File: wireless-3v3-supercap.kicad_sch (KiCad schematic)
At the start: 5 parts

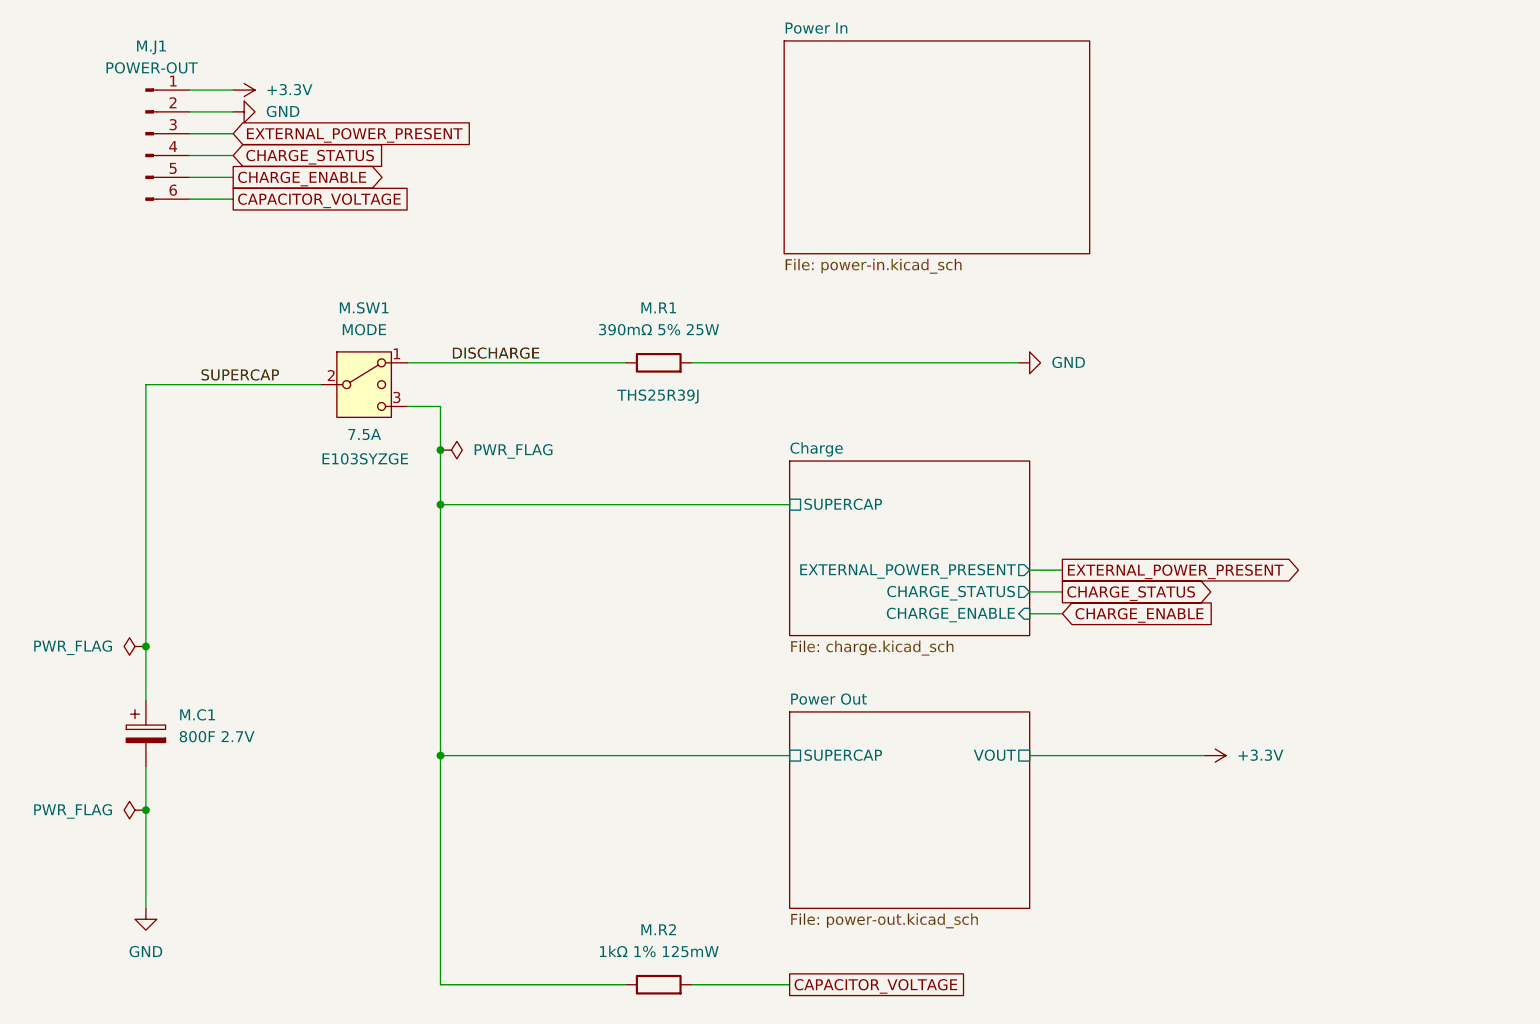
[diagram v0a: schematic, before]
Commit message: Remove charge enable pin
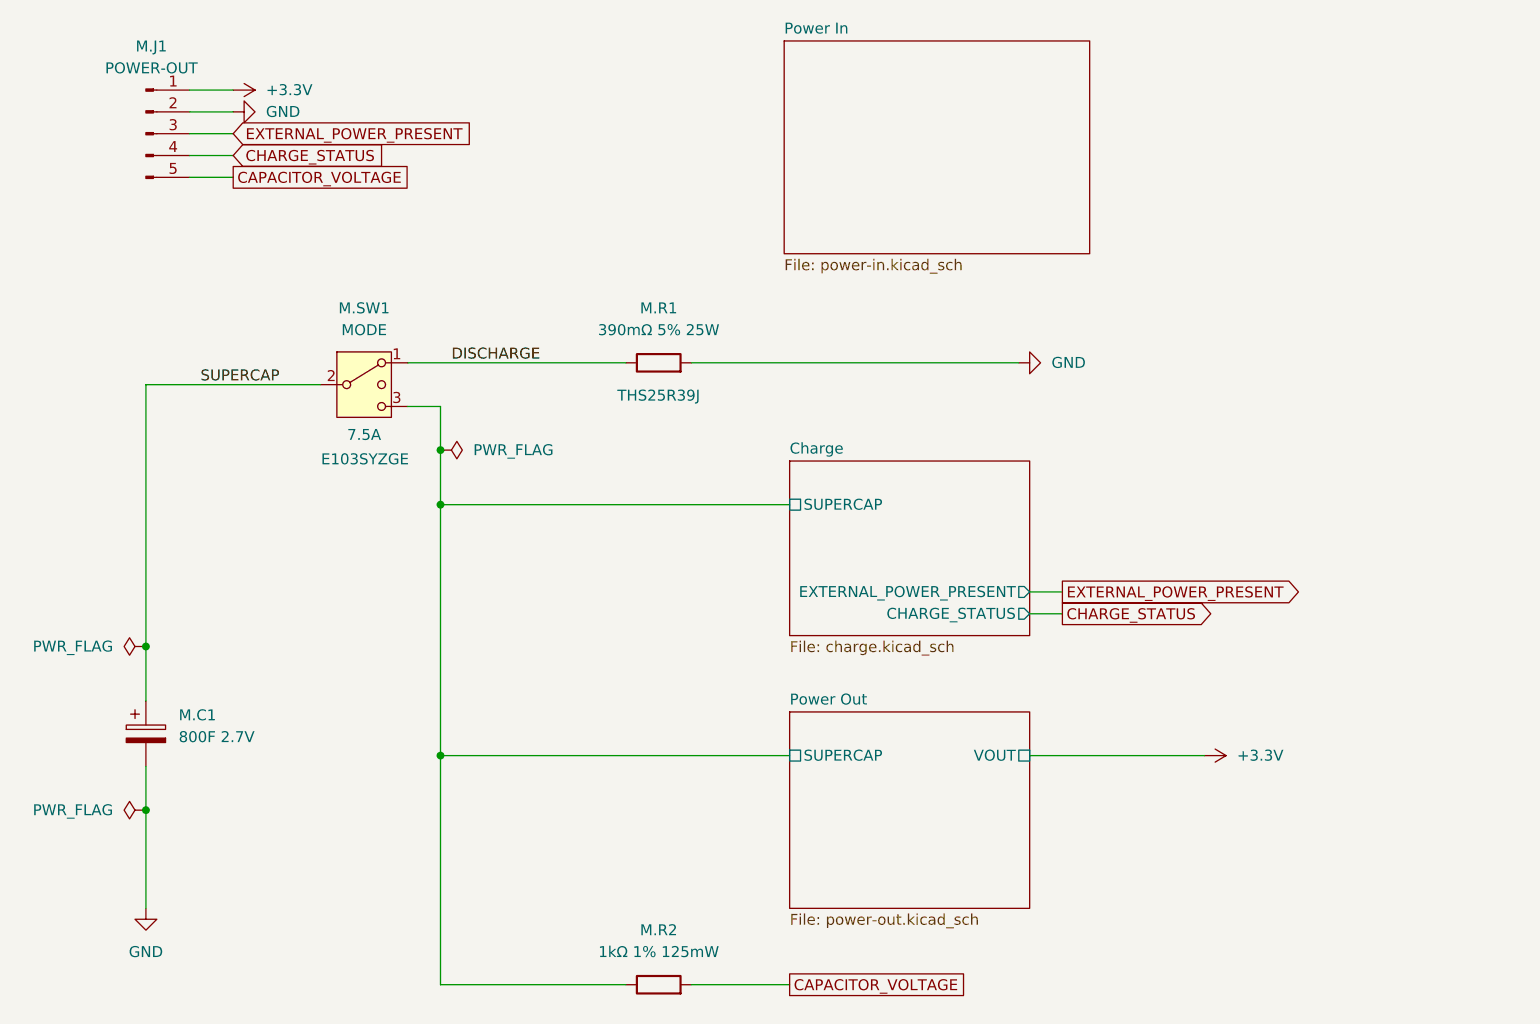
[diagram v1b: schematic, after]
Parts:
- M.J1: footprint Connector_PinHeader_2.54mm:PinHeader_1x06_P2.54mm_Vertical -> Connector_PinHeader_2.54mm:PinHeader_1x05_P2.54mm_Vertical; symbol Connector:Conn_01x06_Pin -> Connector:Conn_01x05_Pin
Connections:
- net CHARGE_ENABLE is gone; now on net CAPACITOR_VOLTAGE: M.J1.5 (Pin_5)
- net CAPACITOR_VOLTAGE: no longer M.J1.6 (Pin_6)
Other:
- sheet Charge ports: added none; removed CHARGE_ENABLE
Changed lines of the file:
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@@
-	(wire
-		(pts
-			(xy 30.48 27.94) (xy 35.56 27.94)
-		)
-		(stroke
-			(width 0)
-			(type default)
-		)
-	)
 	(wire
 		(pts
@@
 	(wire
 		(pts
+			(xy 59.69 63.5) (xy 100.33 63.5)
+		)
+		(stroke
+			(width 0)
+			(type default)
+		)
+	)
+	(wire
+		(pts
+			(xy 30.48 25.4) (xy 35.56 25.4)
+		)
+		(stroke
+			(width 0)
+			(type default)
+		)
+	)
+	(wire
+		(pts
+			(xy 25.4 80.01) (xy 25.4 86.36)
+		)
+		(stroke
+			(width 0)
+			(type default)
+		)
+	)
+	(wire
+		(pts
+			(xy 128.27 73.66) (xy 132.08 73.66)
+		)
+		(stroke
+			(width 0)
+			(type default)
+		)
+	)
+	(wire
+		(pts
+			(xy 30.48 15.24) (xy 35.56 15.24)
+		)
+		(stroke
+			(width 0)
+			(type default)
+		)
+	)
+	(wire
+		(pts
+			(xy 128.27 92.71) (xy 148.59 92.71)
+		)
+		(stroke
+			(width 0)
+			(type default)
+		)
+	)
+	(wire
+		(pts
 			(xy 128.27 76.2) (xy 132.08 76.2)
-		)
-		(stroke
-			(width 0)
-			(type default)
-		)
-	)
-	(wire
-		(pts
-			(xy 59.69 63.5) (xy 100.33 63.5)
-		)
-		(stroke
-			(width 0)
-			(type default)
-		)
-	)
-	(wire
-		(pts
-			(xy 30.48 25.4) (xy 35.56 25.4)
-		)
-		(stroke
-			(width 0)
-			(type default)
-		)
-	)
-	(wire
-		(pts
-			(xy 25.4 80.01) (xy 25.4 86.36)
-		)
-		(stroke
-			(width 0)
-			(type default)
-		)
-	)
-	(wire
-		(pts
-			(xy 128.27 71.12) (xy 132.08 71.12)
-		)
-		(stroke
-			(width 0)
-			(type default)
-		)
-	)
-	(wire
-		(pts
-			(xy 30.48 15.24) (xy 35.56 15.24)
-		)
-		(stroke
-			(width 0)
-			(type default)
-		)
-	)
-	(wire
-		(pts
-			(xy 128.27 92.71) (xy 148.59 92.71)
-		)
-		(stroke
-			(width 0)
-			(type default)
-		)
-	)
-	(wire
-		(pts
-			(xy 128.27 73.66) (xy 132.08 73.66)
 		)
 		(stroke
@@
 		)
 	)
-	(global_label "CHARGE_ENABLE"
-		(shape input)
-		(at 132.08 76.2 0)
+	(global_label "CAPACITOR_VOLTAGE"
+		(shape passive)
+		(at 100.33 119.38 0)
 		(fields_autoplaced yes)
 		(effects
@@
 		)
 		(property "Intersheetrefs" "${INTERSHEET_REFS}"
-			(at 150.4261 76.2 0)
-			(effects
-				(font
-					(size 1.27 1.27)
-				)
-				(justify left)
-				(hide yes)
-			)
-		)
-	)
-	(global_label "CAPACITOR_VOLTAGE"
-		(shape passive)
-		(at 100.33 119.38 0)
+			(at 121.254 119.38 0)
+			(effects
+				(font
+					(size 1.27 1.27)
+				)
+				(justify left)
+				(hide yes)
+			)
+		)
+	)
+	(global_label "EXTERNAL_POWER_PRESENT"
+		(shape output)
+		(at 132.08 73.66 0)
 		(fields_autoplaced yes)
 		(effects
@@
 		)
 		(property "Intersheetrefs" "${INTERSHEET_REFS}"
-			(at 121.254 119.38 0)
-			(effects
-				(font
-					(size 1.27 1.27)
-				)
-				(justify left)
-				(hide yes)
-			)
-		)
-	)
-	(global_label "EXTERNAL_POWER_PRESENT"
-		(shape output)
-		(at 132.08 71.12 0)
+			(at 161.0092 73.66 0)
+			(effects
+				(font
+					(size 1.27 1.27)
+				)
+				(justify left)
+				(hide yes)
+			)
+		)
+	)
+	(global_label "CHARGE_STATUS"
+		(shape input)
+		(at 35.56 22.86 0)
 		(fields_autoplaced yes)
 		(effects
@@
 		)
 		(property "Intersheetrefs" "${INTERSHEET_REFS}"
-			(at 161.0092 71.12 0)
+			(at 53.6642 22.86 0)
 			(effects
 				(font
@@
 	)
 	(global_label "CHARGE_STATUS"
-		(shape input)
-		(at 35.56 22.86 0)
+		(shape output)
+		(at 132.08 76.2 0)
 		(fields_autoplaced yes)
 		(effects
@@
 		)
 		(property "Intersheetrefs" "${INTERSHEET_REFS}"
-			(at 53.6642 22.86 0)
-			(effects
-				(font
-					(size 1.27 1.27)
-				)
-				(justify left)
-				(hide yes)
-			)
-		)
-	)
-	(global_label "CHARGE_STATUS"
-		(shape output)
-		(at 132.08 73.66 0)
+			(at 150.1842 76.2 0)
+			(effects
+				(font
+					(size 1.27 1.27)
+				)
+				(justify left)
+				(hide yes)
+			)
+		)
+	)
+	(global_label "CAPACITOR_VOLTAGE"
+		(shape passive)
+		(at 35.56 25.4 0)
 		(fields_autoplaced yes)
 		(effects
@@
 		)
 		(property "Intersheetrefs" "${INTERSHEET_REFS}"
-			(at 150.1842 73.66 0)
-			(effects
-				(font
-					(size 1.27 1.27)
-				)
-				(justify left)
-				(hide yes)
-			)
-		)
-	)
-	(global_label "CHARGE_ENABLE"
-		(shape output)
-		(at 35.56 25.4 0)
-		(fields_autoplaced yes)
-		(effects
-			(font
-				(size 1.27 1.27)
-			)
-			(justify left)
-		)
-		(property "Intersheetrefs" "${INTERSHEET_REFS}"
-			(at 53.9061 25.4 0)
-			(effects
-				(font
-					(size 1.27 1.27)
-				)
-				(justify left)
-				(hide yes)
-			)
-		)
-	)
-	(global_label "CAPACITOR_VOLTAGE"
-		(shape passive)
-		(at 35.56 27.94 0)
-		(fields_autoplaced yes)
-		(effects
-			(font
-				(size 1.27 1.27)
-			)
-			(justify left)
-		)
-		(property "Intersheetrefs" "${INTERSHEET_REFS}"
-			(at 56.484 27.94 0)
+			(at 56.484 25.4 0)
 			(effects
 				(font
@@
 	)
 	(symbol
-		(lib_id "Connector:Conn_01x06_Pin")
+		(lib_id "Connector:Conn_01x05_Pin")
 		(at 25.4 20.32 0)
 		(unit 1)
@@
 			)
 		)
-		(property "Footprint" "Connector_PinHeader_2.54mm:PinHeader_1x06_P2.54mm_Vertical"
+		(property "Footprint" "Connector_PinHeader_2.54mm:PinHeader_1x05_P2.54mm_Vertical"
 			(at 25.4 20.32 0)
 			(effects
@@
 			)
 		)
-		(property "Description" "Generic connector, single row, 01x06, script generated"
+		(property "Description" "Generic connector, single row, 01x05, script generated"
 			(at 25.4 20.32 0)
 			(effects
@@
 		)
 		(pin "5"
-		)
-		(pin "6"
 		)
 		(instances
@@
 			)
 		)
-		(pin "CHARGE_ENABLE" input
+		(pin "CHARGE_STATUS" output
 			(at 128.27 76.2 0)
 			(effects
@@
 			)
 		)
-		(pin "CHARGE_STATUS" output
+		(pin "EXTERNAL_POWER_PRESENT" output
 			(at 128.27 73.66 0)
 			(effects
 				(font
-					(size 1.27 1.27)
-				)
-				(justify right)
-			)
-		)
-		(pin "EXTERNAL_POWER_PRESENT" output
-			(at 128.27 71.12 0)
-			(effects
-				(font

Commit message: Add voltage divider circuit for ADC
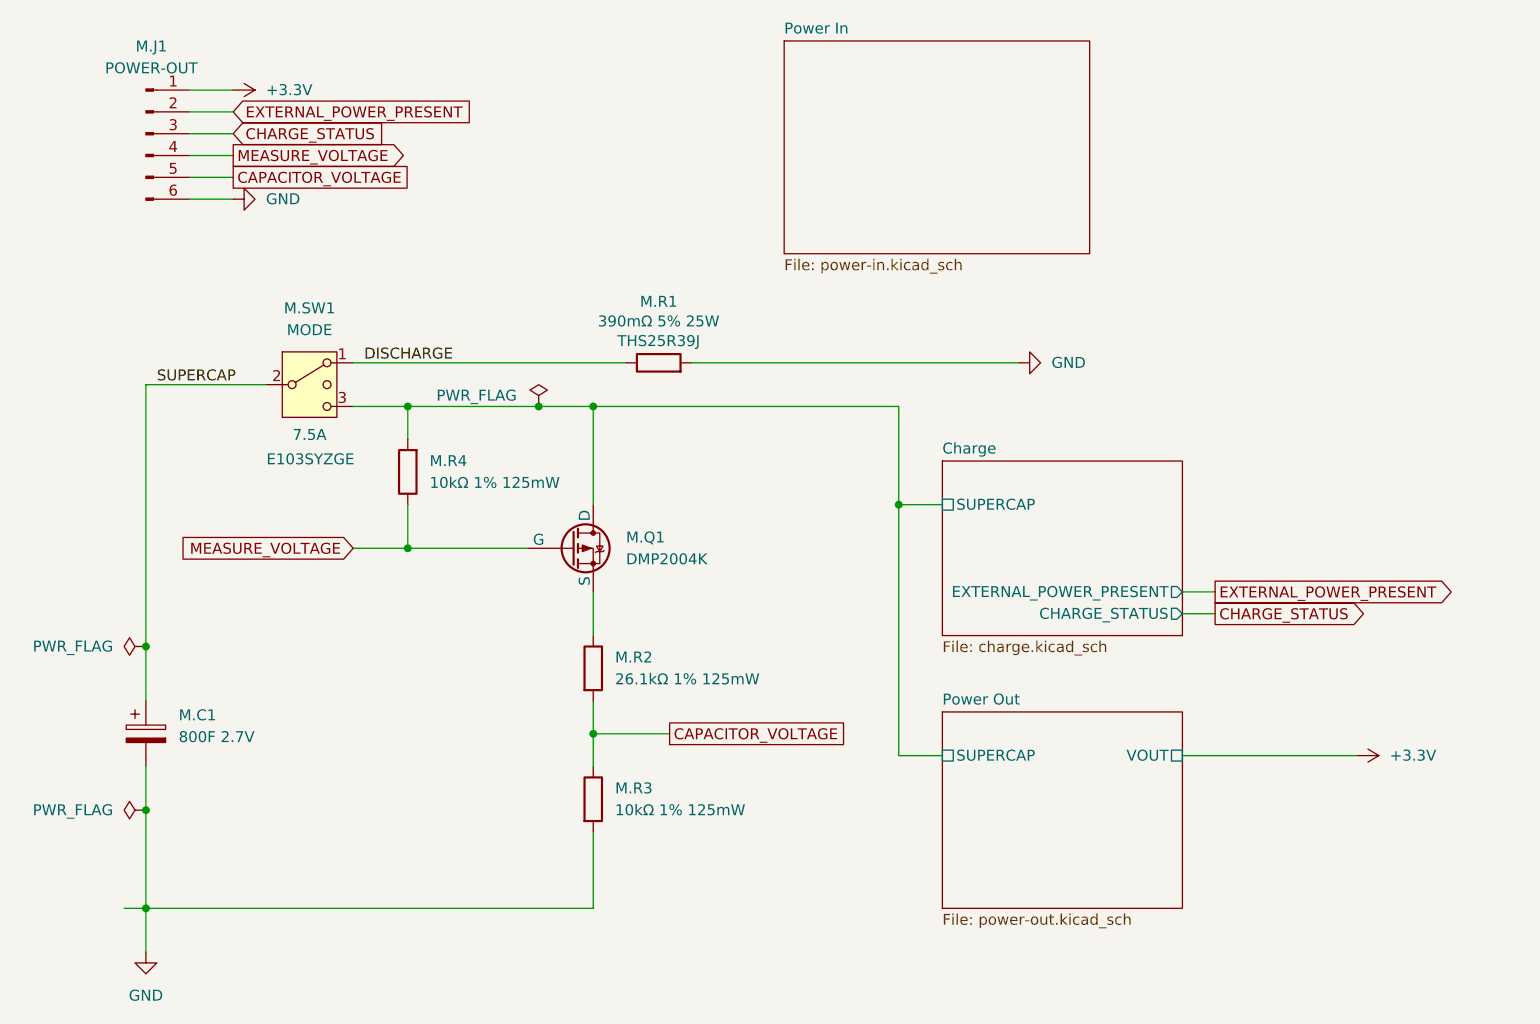
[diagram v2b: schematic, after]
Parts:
- added M.Q1: DMP2004K, Package_TO_SOT_SMD:SOT-23, symbol Simulation_SPICE:PMOS
- added M.R3, M.R4: 10kΩ 1% 125mW, Resistor_SMD:R_0805_2012Metric_Pad1.20x1.40mm_HandSolder, symbol Device:R
- M.J1: footprint Connector_PinHeader_2.54mm:PinHeader_1x05_P2.54mm_Vertical -> Connector_PinHeader_2.54mm:PinHeader_1x06_P2.54mm_Vertical; symbol Connector:Conn_01x05_Pin -> Connector:Conn_01x06_Pin
- M.R2: value 1kΩ 1% 125mW -> 26.1kΩ 1% 125mW
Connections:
- net CAPACITOR_VOLTAGE: now also M.R3.1
- net CHARGE_STATUS: now also M.J1.3 (Pin_3); no longer M.J1.4 (Pin_4)
- net Charge/SUPERCAP: now also M.Q1.3 (D), M.R4.2; no longer M.R2.1
- net EXTERNAL_POWER_PRESENT: now also M.J1.2 (Pin_2); no longer M.J1.3 (Pin_3)
- net GND: now also M.J1.6 (Pin_6), M.R3.2; no longer M.J1.2 (Pin_2)
- new net: M.Q1.2 (S), M.R2.1
- new net MEASURE_VOLTAGE: M.J1.4 (Pin_4), M.Q1.1 (G), M.R4.1
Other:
- moved on the sheet: M.R2, M.SW1

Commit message: Fix MOSFET for measuring capacitor voltage
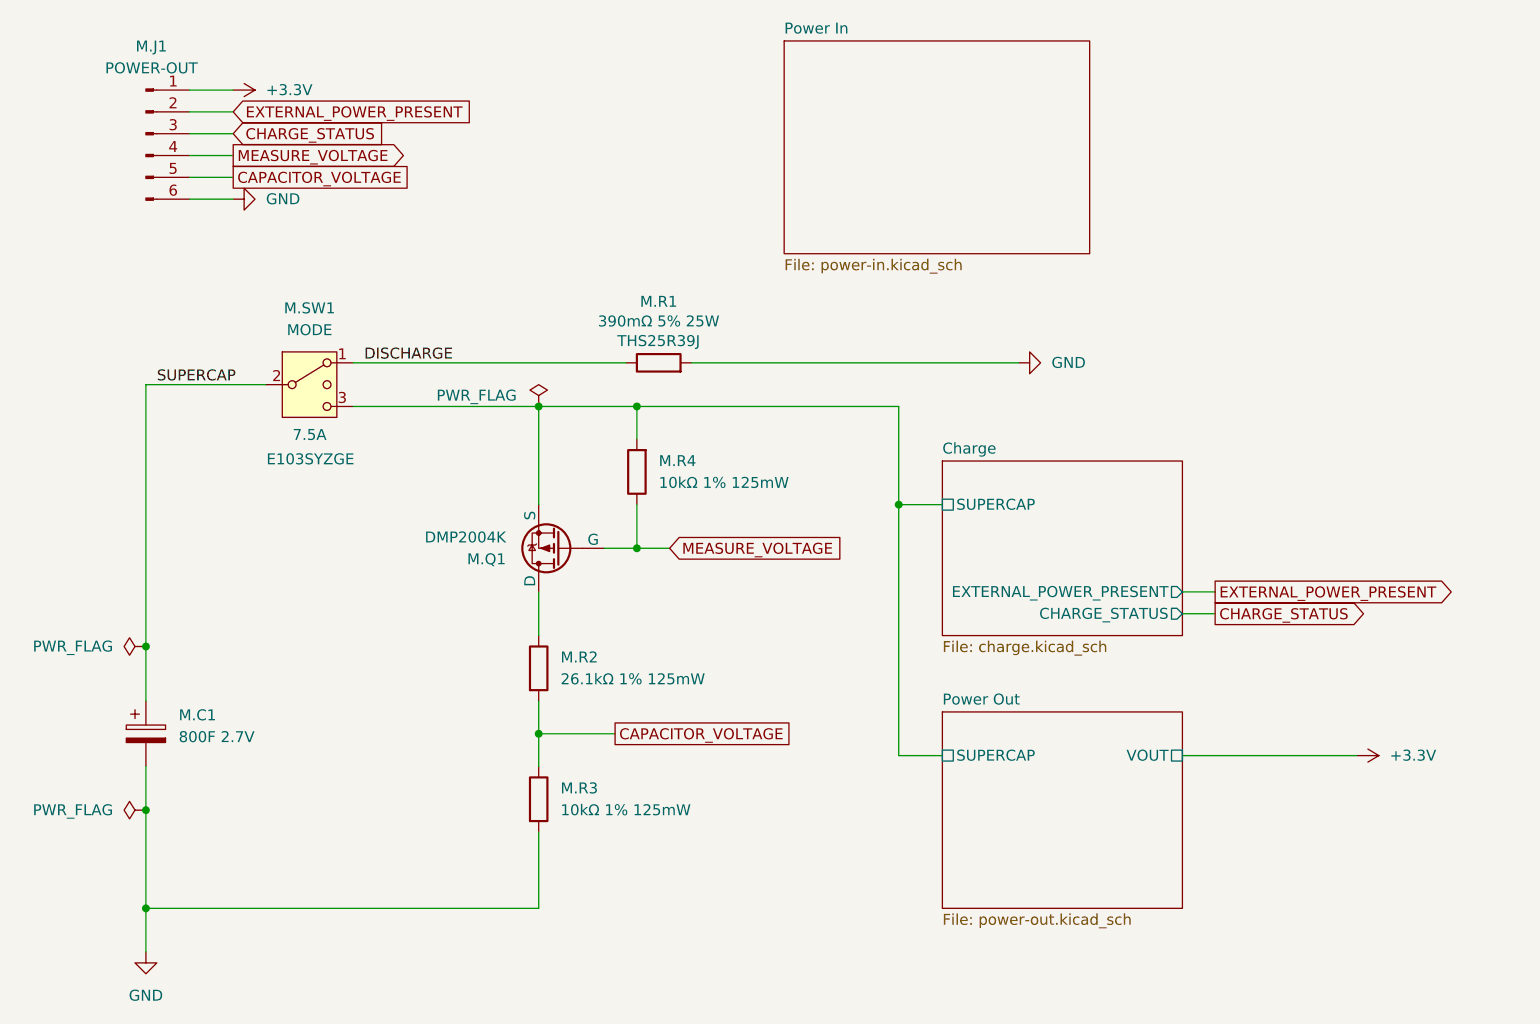
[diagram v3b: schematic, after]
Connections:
- net Charge/SUPERCAP: now also M.Q1.2 (S); no longer M.Q1.3 (D)
- net at M.R2.1: now also M.Q1.3 (D); no longer M.Q1.2 (S)
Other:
- moved on the sheet: M.Q1, M.R2, M.R3, M.R4
